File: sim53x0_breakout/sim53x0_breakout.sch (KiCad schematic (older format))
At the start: 39 parts, among them J1 CONN_01X05, J2 USB_OTG, J3 SIM_Card, J4 CONN_01X06, J5 CONN_COAXIAL, J8 CONN_COAXIAL, J9 CONN_COAXIAL, U1 SIM5320

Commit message: Adding u.FL to SIM53x0 board - no antenna traces yet
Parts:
- J5, J8, J9: footprint (none) -> footprints:HRS_U.FL-R-SMT(01)
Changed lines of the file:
@@
 F 0 "J8" H 6860 4720 50  0000 C CNN
 F 1 "CONN_COAXIAL" H 7250 4650 50  0000 C CNN
-F 2 "" H 6850 4600 50  0001 C CNN
+F 2 "footprints:HRS_U.FL-R-SMT(01)" H 6850 4600 50  0001 C CNN
 F 3 "" H 6850 4600 50  0001 C CNN
 	1    6850 4600
@@
 F 0 "J9" H 6960 2820 50  0000 C CNN
 F 1 "CONN_COAXIAL" H 7350 2750 50  0000 C CNN
-F 2 "" H 6950 2700 50  0001 C CNN
+F 2 "footprints:HRS_U.FL-R-SMT(01)" H 6950 2700 50  0001 C CNN
 F 3 "" H 6950 2700 50  0001 C CNN
 	1    6950 2700
@@
 F 0 "J5" H 3660 1220 50  0000 C CNN
 F 1 "CONN_COAXIAL" V 3800 900 50  0000 C CNN
-F 2 "" H 3650 1100 50  0001 C CNN
+F 2 "footprints:HRS_U.FL-R-SMT(01)" H 3650 1100 50  0001 C CNN
 F 3 "" H 3650 1100 50  0001 C CNN
 	1    3650 1100
@@
 Connection ~ 6800 4200
 $Comp
-L GND #PWR035
+L GND #PWR034
 U 1 1 59635C5B
 P 3000 3000
-F 0 "#PWR035" H 3000 2750 50  0001 C CNN
+F 0 "#PWR034" H 3000 2750 50  0001 C CNN
 F 1 "GND" V 3000 2800 50  0000 C CNN
 F 2 "" H 3000 3000 50  0001 C CNN
@@
 $EndComp
 $Comp
-L GND #PWR036
+L GND #PWR035
 U 1 1 596387AC
 P 7150 3500
-F 0 "#PWR036" H 7150 3250 50  0001 C CNN
+F 0 "#PWR035" H 7150 3250 50  0001 C CNN
 F 1 "GND" V 7150 3300 50  0000 C CNN
 F 2 "" H 7150 3500 50  0001 C CNN
@@
 $EndComp
 $Comp
-L GND #PWR037
+L GND #PWR036
 U 1 1 5962BC6C
 P 2150 2800
-F 0 "#PWR037" H 2150 2550 50  0001 C CNN
+F 0 "#PWR036" H 2150 2550 50  0001 C CNN
 F 1 "GND" V 2150 2600 50  0000 C CNN
 F 2 "" H 2150 2800 50  0001 C CNN
@@
 Connection ~ 2550 2800
 $Comp
-L GND #PWR038
+L GND #PWR037
 U 1 1 5962D9EA
 P 6850 4800
-F 0 "#PWR038" H 6850 4550 50  0001 C CNN
+F 0 "#PWR037" H 6850 4550 50  0001 C CNN
 F 1 "GND" H 6850 4650 50  0000 C CNN
 F 2 "" H 6850 4800 50  0001 C CNN
@@
 $EndComp
 $Comp
-L GND #PWR039
+L GND #PWR038
 U 1 1 5962DA70
 P 6950 2900
-F 0 "#PWR039" H 6950 2650 50  0001 C CNN
+F 0 "#PWR038" H 6950 2650 50  0001 C CNN
 F 1 "GND" H 6950 2750 50  0000 C CNN
 F 2 "" H 6950 2900 50  0001 C CNN
@@
 $EndComp
 $Comp
-L GND #PWR040
+L GND #PWR039
 U 1 1 59A9D276
 P 1700 4100
-F 0 "#PWR040" H 1700 3850 50  0001 C CNN
+F 0 "#PWR039" H 1700 3850 50  0001 C CNN
 F 1 "GND" H 1700 3950 50  0000 C CNN
 F 2 "" H 1700 4100 50  0001 C CNN

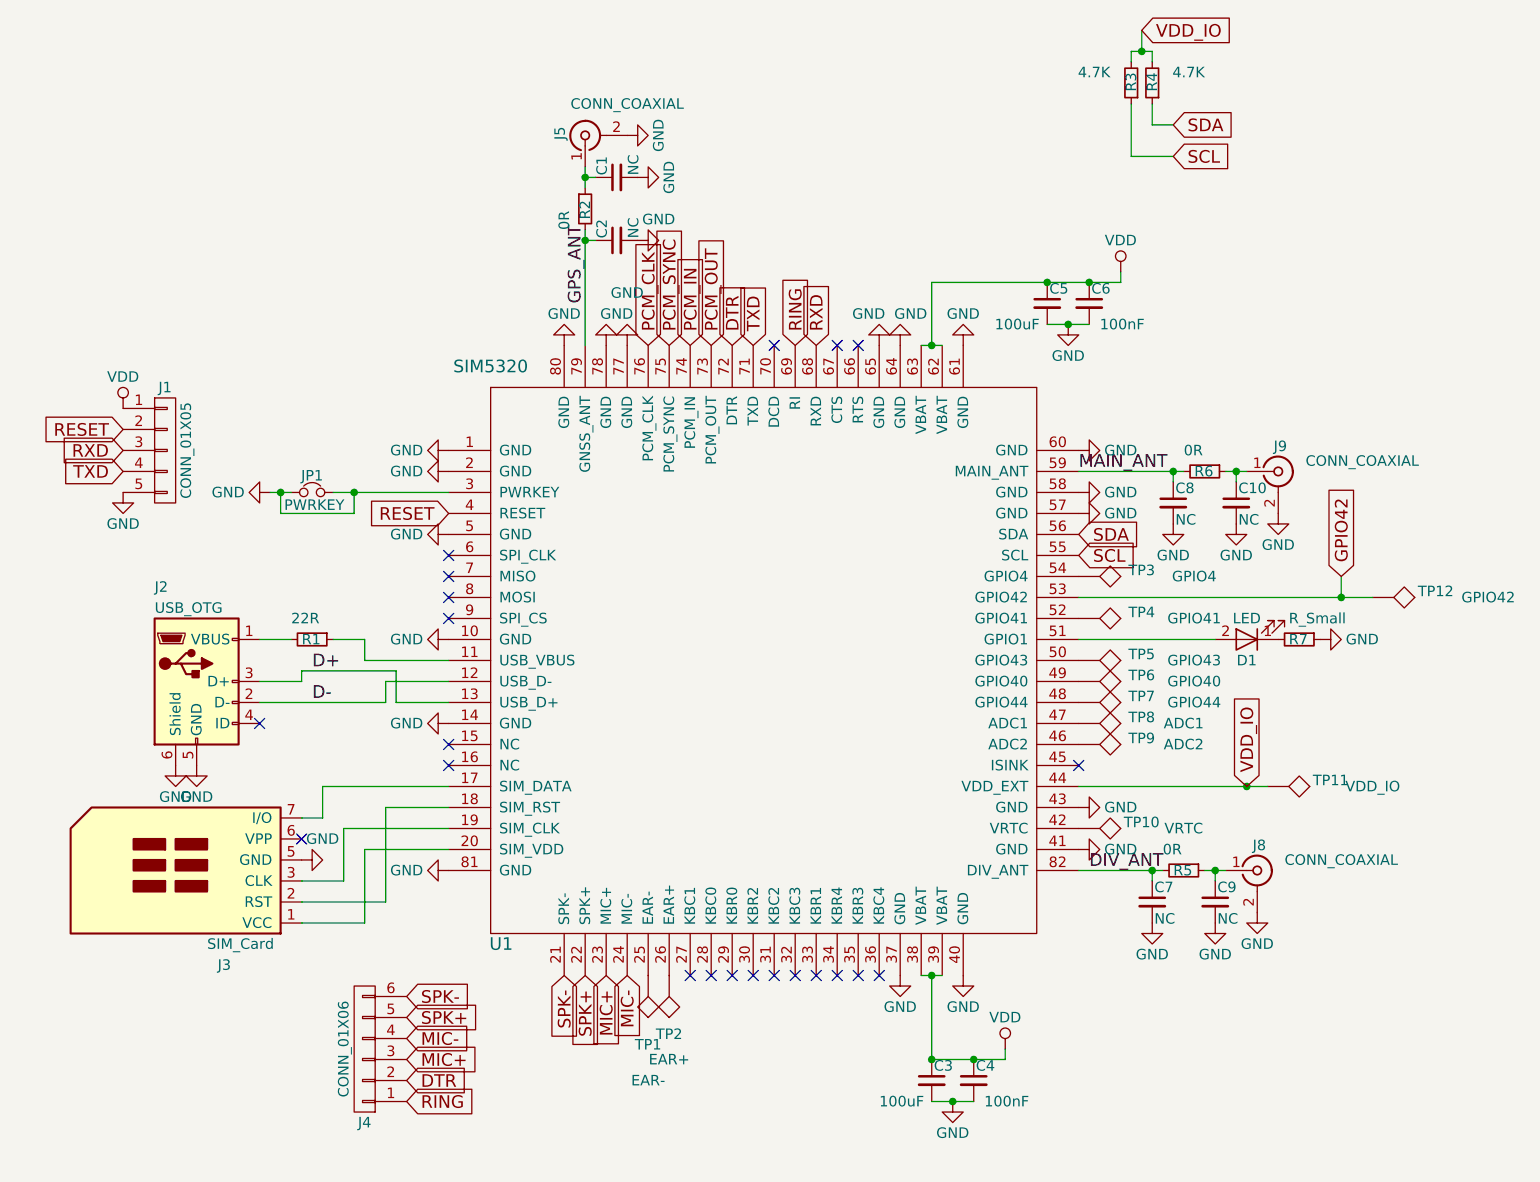
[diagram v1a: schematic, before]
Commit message: New version of the SIM5X30 breakout - adjusted for Delta boards
Needs to be printed out to see clearances
No SIM slot footprint yet
No SIM5320, u.FL and SIM slot 3D models
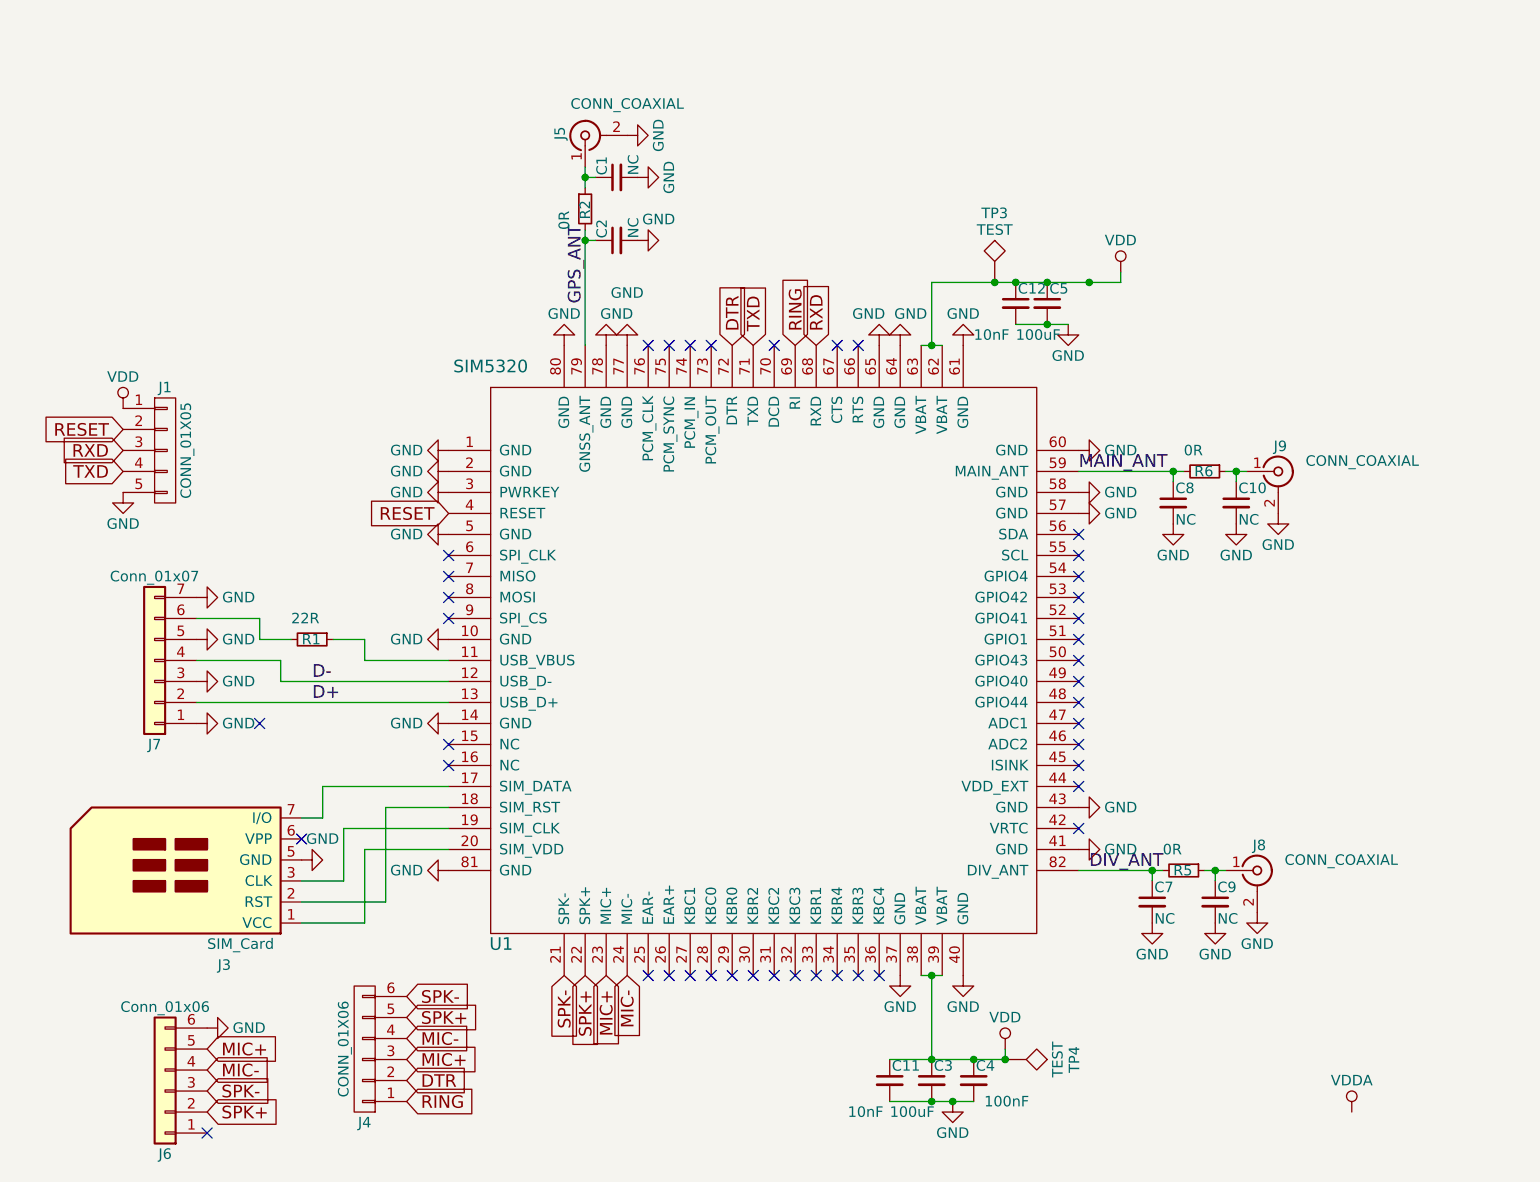
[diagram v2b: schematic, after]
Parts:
- removed C6: 100nF, Capacitors_SMD:C_0805_HandSoldering, symbol C_Small
- removed D1: LED, Resistors_SMD:R_0603, symbol LED
- removed J2: USB_OTG, footprints:MICROUSB_SIMPLE, symbol USB_OTG
- removed JP1: PWRKEY, footprints:GS2_SMALL, symbol Jumper_NC_Small
- removed R3, R4: 4.7K, Resistors_SMD:R_0603_HandSoldering, symbol R_Small
- removed R7: R_Small, Resistors_SMD:R_0603, symbol R_Small
- removed TP1: EAR-, Measurement_Points:Measurement_Point_Square-SMD-Pad_Small, symbol TEST
- removed TP10: VRTC, Measurement_Points:Measurement_Point_Square-SMD-Pad_Small, symbol TEST
- removed TP11: VDD_IO, Measurement_Points:Measurement_Point_Square-SMD-Pad_Small, symbol TEST
- removed TP12: GPIO42, Measurement_Points:Measurement_Point_Square-SMD-Pad_Small, symbol TEST
- removed TP2: EAR+, Measurement_Points:Measurement_Point_Square-SMD-Pad_Small, symbol TEST
- removed TP5: GPIO43, Measurement_Points:Measurement_Point_Square-SMD-Pad_Small, symbol TEST
- removed TP6: GPIO40, Measurement_Points:Measurement_Point_Square-SMD-Pad_Small, symbol TEST
- removed TP7: GPIO44, Measurement_Points:Measurement_Point_Square-SMD-Pad_Small, symbol TEST
- removed TP8: ADC1, Measurement_Points:Measurement_Point_Square-SMD-Pad_Small, symbol TEST
- removed TP9: ADC2, Measurement_Points:Measurement_Point_Square-SMD-Pad_Small, symbol TEST
- added C11, C12: 10nF, Capacitors_Tantalum_SMD:CP_Tantalum_Case-B_EIA-3528-21_Reflow, symbol C_Small
- added J6: Conn_01x06, Pin_Headers:Pin_Header_Straight_1x06_Pitch2.54mm, symbol Conn_01x06
- added J7: Conn_01x07, Connectors_JST:JST_SH_BM06B-SRSS-TB_06x1.00mm_Straight, symbol Conn_01x07
- C3, C5: footprint Capacitors_Tantalum_SMD:CP_Tantalum_Case-D_EIA-7343-31_Hand -> Capacitors_Tantalum_SMD:CP_Tantalum_Case-D_EIA-7343-31_Reflow
- C4: footprint Capacitors_SMD:C_0805_HandSoldering -> Capacitors_SMD:C_0805
- J1: footprint Pin_Headers:Pin_Header_Straight_1x05_Pitch2.54mm -> Pin_Headers:Pin_Header_Straight_1x05_Pitch2.54mm_SMD_Pin1Left
- J4: footprint Pin_Headers:Pin_Header_Straight_1x06_Pitch2.54mm -> Pin_Headers:Pin_Header_Straight_1x06_Pitch2.54mm_SMD_Pin1Left
- TP3: value GPIO4 -> TEST; footprint Measurement_Points:Measurement_Point_Square-SMD-Pad_Small -> Pin_Headers:Pin_Header_Straight_1x01_Pitch2.54mm
- TP4: value GPIO41 -> TEST; footprint Measurement_Points:Measurement_Point_Square-SMD-Pad_Small -> Pin_Headers:Pin_Header_Straight_1x01_Pitch2.54mm
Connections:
- net D+: now also J7.2 (Pin_2)
- net D-: now also J7.4 (Pin_4)
- net GND: now also C11.2, C12.2, J6.6 (Pin_6), J7.1 (Pin_1), J7.3 (Pin_3), J7.5 (Pin_5), J7.7 (Pin_7)
- net MIC+: now also J6.5 (Pin_5)
- net MIC-: now also J6.4 (Pin_4)
- net SPK+: now also J6.2 (Pin_2)
- net SPK-: now also J6.3 (Pin_3)
- net VDD: now also TP3.1, TP4.1, C11.1, C12.1
- net at U1.52 (GPIO41): no longer TP4.1
- net at U1.54 (GPIO4): no longer TP3.1
- net at R1.2: now also J7.6 (Pin_6)
- net GPIO42: no longer names the net of U1.53 (GPIO42)
- net PCM_CLK: no longer names the net of U1.76 (PCM_CLK)
- net PCM_IN: no longer names the net of U1.74 (PCM_IN)
- net PCM_OUT: no longer names the net of U1.73 (PCM_OUT)
- net PCM_SYNC: no longer names the net of U1.75 (PCM_SYNC)
- net SCL: no longer names the net of U1.55 (SCL)
- net SDA: no longer names the net of U1.56 (SDA)
- net VDD_IO: no longer names the net of U1.44 (VDD_EXT)
- no-connect marks 22 -> 42

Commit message: Finished board - has limited usability! 3G modem too big
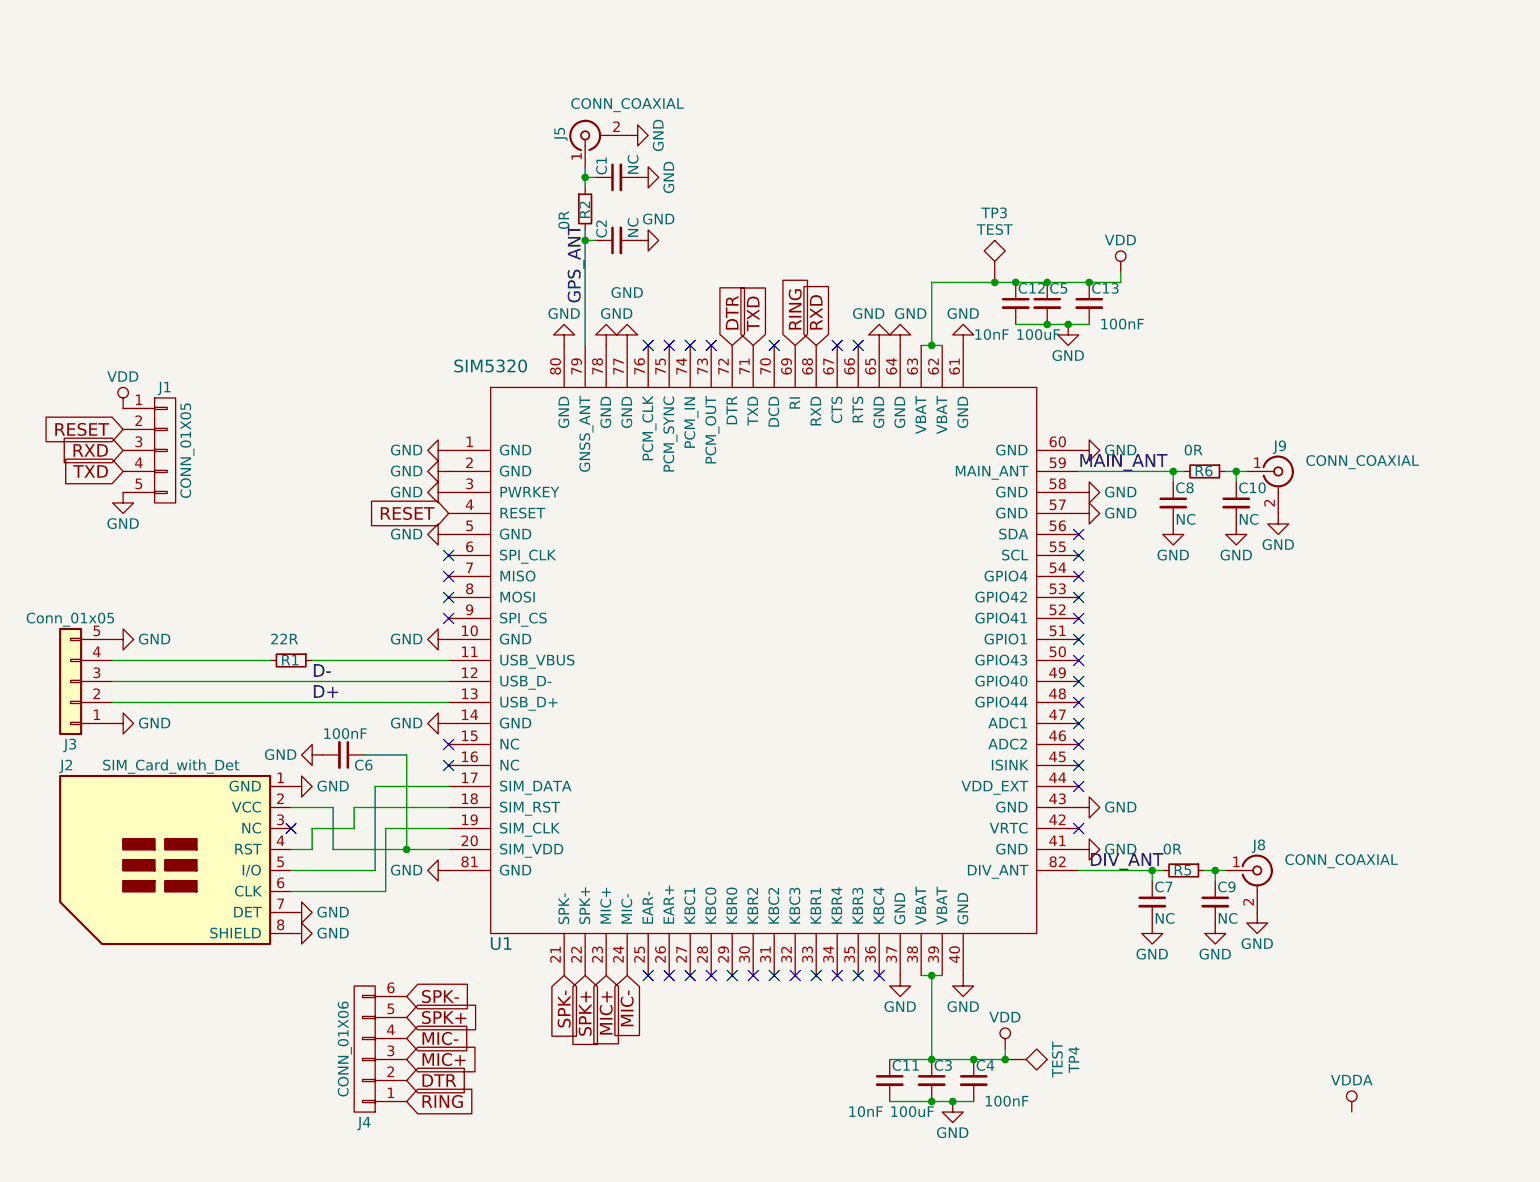
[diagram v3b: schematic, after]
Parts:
- removed J3: SIM_Card, symbol SIM_Card
- removed J6: Conn_01x06, Pin_Headers:Pin_Header_Straight_1x06_Pitch2.54mm, symbol Conn_01x06
- removed J7: Conn_01x07, Connectors_JST:JST_SH_BM06B-SRSS-TB_06x1.00mm_Straight, symbol Conn_01x07
- added C13, C6: 100nF, Capacitors_SMD:C_0805, symbol C_Small
- added J2: SIM_Card_with_Det, footprints:MICROSIM_6P_SMD_HOLDER, symbol SIM_Card_with_Det
- added J3: Conn_01x05, Connectors_JST:JST_SH_BM04B-SRSS-TB_04x1.00mm_Straight, symbol Conn_01x05
- J1: footprint Pin_Headers:Pin_Header_Straight_1x05_Pitch2.54mm_SMD_Pin1Left -> footprints:Pin_Header_Straight_1x05_Pitch2.54mm_SMD
- J4: footprint Pin_Headers:Pin_Header_Straight_1x06_Pitch2.54mm_SMD_Pin1Left -> footprints:Pin_Header_Straight_1x06_Pitch2.54mm_SMD
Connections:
- net D+: now also J3.2 (Pin_2)
- net D-: now also J3.3 (Pin_3)
- net GND: now also C13.2, C6.2, J2.1 (GND), J2.7 (DET), J2.8 (SHIELD), J3.1 (Pin_1), J3.5 (Pin_5)
- net VDD: now also C13.1
- net at U1.17 (SIM_DATA): now also J2.5 (I/O)
- net at U1.18 (SIM_RST): now also J2.4 (RST)
- net at U1.19 (SIM_CLK): now also J2.6 (CLK)
- net at U1.20 (SIM_VDD): now also C6.1, J2.2 (VCC)
- net at R1.2: now also J3.4 (Pin_4)
- no-connect marks 42 -> 40
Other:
- moved on the sheet: R1
